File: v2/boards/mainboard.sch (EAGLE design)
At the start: 176 parts, among them IC1 LM2596S-ADJ, IC10 TSOP34830, IC11 DRV8835, IC12 ESP-WROOM-32, IC13 PAM8403, IC2 LM2596S-5.0, IC3 LD1117A, IC4 LM393, IC5 MCP101-300, IC6 TEENSY 3.6, IC7 PCA9634, IC8 PCA9554, IC9 PCA9634, J1 Bat_In, J10 SPI_0, J11 SPI_2, J12 SPI_2, J13 I2C_0, J14 I2C_1, J15 I2C_3, J16 BNO055, J17 Uart_2, J18 Uart_5, J19 Uart_6 (LP), J2 Erw_Pow, J20 BPS, J21 Servo_2, J22 Servo_3, J23 Erw_Servo, J24 Erw_PWM, J25 ESP32_Uart, J26 SPEAKER_L, J27 SPEAKER_R, J28 AUDIO_TEENSY, J29 SWD, J3 I2C0_5V, J30 SWD_KL02, J31 Erw_ENA, J32 Erw_GPIO, J33 Erw_analog, J34 USB_Host, J35 ESP32_PROG, J4 I2C3_5V, J5 Servo_1, J6 H-Bridge Mode, J7 RC5_SEL, J8 SPI_0, J9 SPI_0, SW1 TL32PO, U1 IRL3103, U4 BS108, U5 BS108, U6 BS108, U7 BS108, U8 BS108, U9 BS108, X1 max. 18V

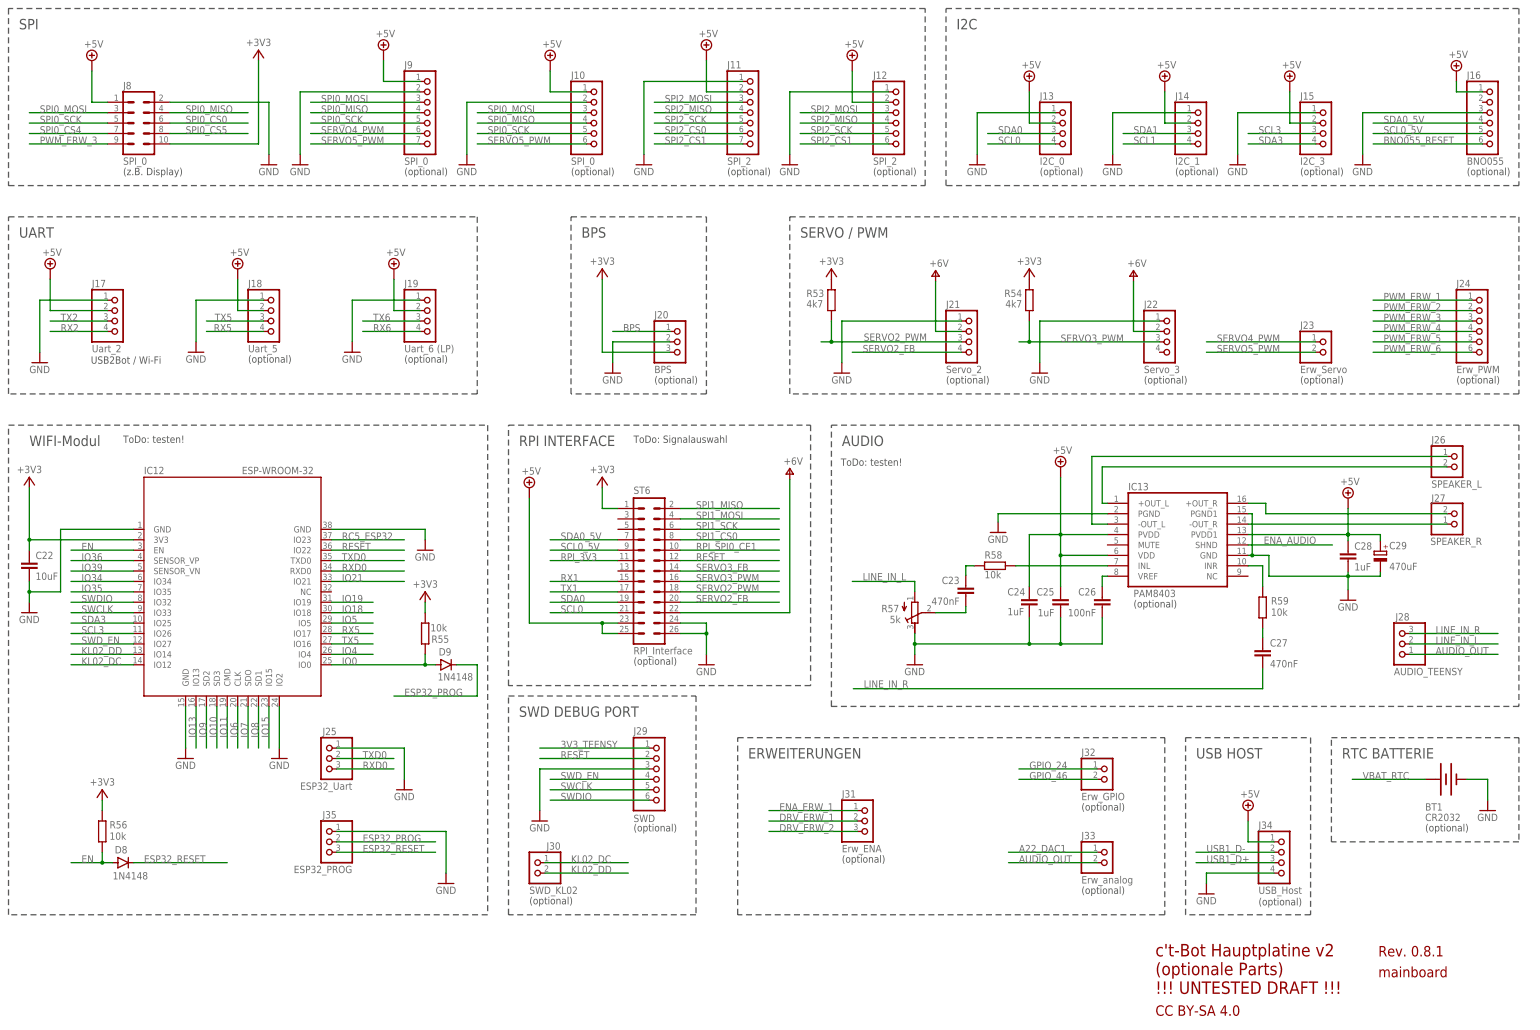
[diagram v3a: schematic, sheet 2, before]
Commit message: ct-bot v2 schematic updated
- optional current measurements added to mainboard
 - schematic drafts for sensor boards
 - pin mapping sheet updated (i2c-bus mapping)
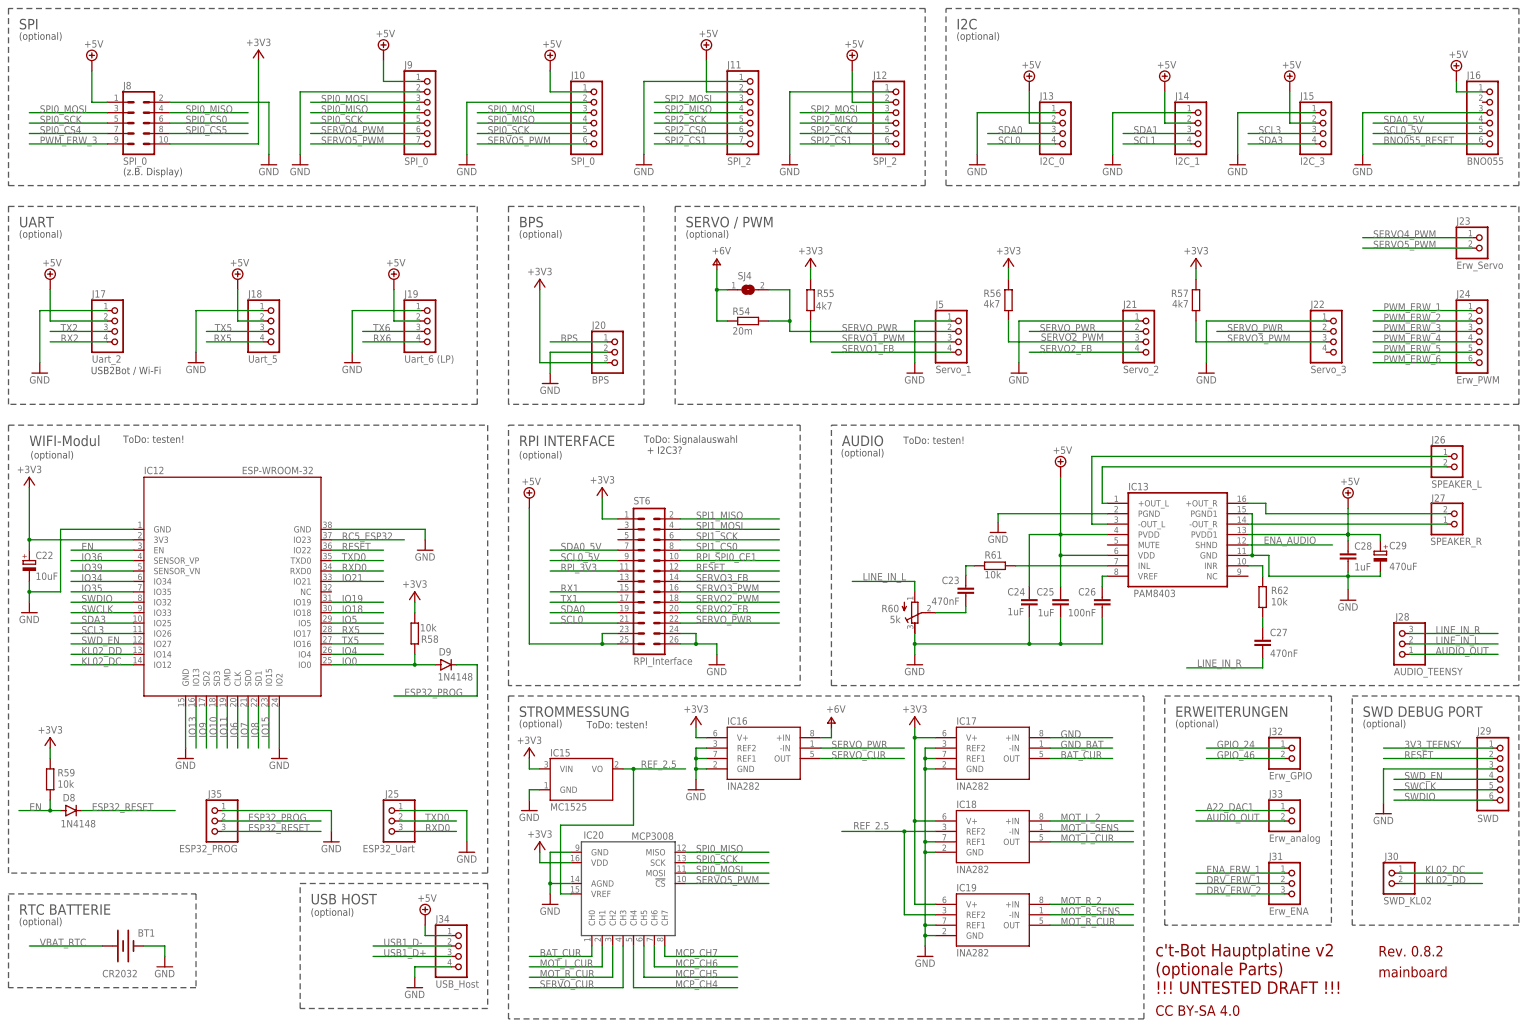
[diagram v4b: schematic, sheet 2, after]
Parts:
- added IC15: MC1525, ct-bot:MC1525TO
- added IC16, IC17, IC18, IC19: INA282, ct-bot:INA28AID
- added IC20: MCP3008, ct-bot:MCP3008SL
- added R51: 4k7, rcl:R-EU_0204/2V
- added R60: 5k, ct-bot:R-TRIMM64W
- added R61: 10k, rcl:R-EU_0204/2V
- added R62: 10k, rcl:R-EU_0204/7
- added SJ1, SJ2, SJ3, SJ4: (no value), jumper:SJ
- C22: device rcl:C-EU025-025X050 -> rcl:CPOL-EUE2.5-5
- J2: value Erw_Pow -> Erw_Pwr
- R10: value 180 -> 120
- R12, R16: value 47k -> 180
- R14, R18: value 180 -> 47k
- R20: value 5k -> 180; device ct-bot:R-TRIMM64W -> rcl:R-EU_0204/2V
- R21: value 10k -> 5k; device rcl:R-EU_0204/2V -> ct-bot:R-TRIMM64W
- R22, R28: value 1M -> 10k
- R23, R29: value 10k -> 1M
- R25, R31: value 15k -> 10k
- R26: value 5k -> 15k; device ct-bot:R-TRIMM64W -> rcl:R-EU_0204/2V
- R27: value 10k -> 5k; device rcl:R-EU_0204/7 -> ct-bot:R-TRIMM64W
- R32: value 100 -> 15k; device rcl:R-EU_0204/2V -> rcl:R-EU_0204/7
- R33: value 470k -> 100
- R35: value 4k7 -> 470k
- R37, R55, R56: value 10k -> 4k7
- R39: value 1k1 -> 10k
- R41: value 1k8 -> 1k1
- R43, R49: value 4k7 -> 1k8
- R44: value 3k9 -> 4k7
- R45: value 220 -> 3k9
- R46: value 590 -> 220
- R47: value 115 -> 590
- R48: value 1k8 -> 115
- R5: value 3k9 0.1% -> 20m; device rcl:R-EU_0204/2V -> rcl:R-EU_R1210
- R52, R53, R54: value 4k7 -> 20m; device rcl:R-EU_0204/2V -> rcl:R-EU_R1210
- R57: value 5k -> 4k7; device ct-bot:R-TRIMM64W -> rcl:R-EU_0204/2V
- R59: device rcl:R-EU_0204/7 -> rcl:R-EU_0204/2V
- R6: value 1k 0.1% -> 3k9 0.1%
- R7: value 390 -> 1k 0.1%
- R8: value 330 -> 390
- R9: value 120 -> 330
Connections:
- new net BAT_CUR: IC17.OUT, IC20.CH0
- new net GND_BAT: IC17.-IN, R5.2, SJ1.2, U1.S
- new net MCP_CH4: IC20.CH4
- new net MCP_CH5: IC20.CH5
- new net MCP_CH6: IC20.CH6
- new net MCP_CH7: IC20.CH7
- new net MOT_L_CUR: IC18.OUT, IC20.CH1
- new net MOT_L_SENS: IC18.-IN, R53.2, SJ3.2, ST5.2
- new net MOT_R_CUR: IC19.OUT, IC20.CH2
- new net MOT_R_SENS: IC19.-IN, R52.2, SJ2.2, ST4.2
- new net REF_2.5: IC15.VO, IC18.REF2, IC19.REF2, IC20.VREF
- new net SERVO_CUR: IC16.OUT, IC20.CH3
- new net SERVO_PWR: IC16.-IN, J21.2, J22.2, J5.2, R54.2, SJ4.2, ST6.22
- net +3V3: now also C22.+, IC15.VIN, IC16.V+, IC17.V+, IC18.V+, IC19.V+, IC20.VDD, R10.2, R13.2, R14.1, R18.2, R21.E, R24.2, R26.2, R27.E, R30.2, R37.2, R41.2, R55.2, R57.2, R58.1, R59.2; no longer C22.1, R12.2, R13.1, R16.2, R20.E, R23.2, R25.2, R26.E, R29.2, R31.2, R39.2, R52.2, R53.2, R54.2, R55.1, R9.2
- net +5V: now also R39.2, R43.2, R51.1, R9.2; no longer R37.2, R41.2, R43.1, R8.2
- net +6V: now also IC16.+IN, R54.1, R6.2, R8.1, SJ4.1; no longer J21.2, J22.2, J5.2, R5.2, R7.1, ST6.22
- net DRV_KANTLED_L: now also R12.2; no longer R11.2
- net DRV_KANTLED_R: now also R16.1; no longer R15.1
- net DRV_LINE_L: now also R20.2; no longer R19.2
- net DRV_LINE_R: now also R19.2; no longer R18.2
- net DRV_RADLED_L: now also R11.2; no longer R10.2
- net DRV_RADLED_R: now also R15.1; no longer R14.1
- net EN: now also R59.1; no longer R56.1
- net ENC_L: now also R25.2, R26.1; no longer R24.2, R25.1
- net ENC_R: now also R31.2, R32.1; no longer R30.2, R31.1
- net GND: now also C22.-, IC15.GND, IC16.GND, IC16.REF1, IC16.REF2, IC17.+IN, IC17.GND, IC17.REF1, IC17.REF2, IC18.GND, IC18.REF1, IC19.GND, IC19.REF1, IC20.AGND, IC20.GND, R21.A, R27.A, R5.1, R60.E, R7.1, SJ1.1; no longer C22.2, R20.A, R26.A, R57.E, R6.1, U1.S
- net IO0: now also R58.2; no longer R55.2
- net KANTE_L: now also R13.1; no longer R12.1
- net KANTE_R: now also R14.2; no longer R13.2
- net LDR_L: now also R34.1; no longer R33.1
- net LDR_R: now also R35.1; no longer R34.1
- net LINE_IN_L: now also R60.A; no longer R57.A
- net LINIE_L: now also R18.1; no longer R17.1
- net LINIE_R: now also R17.1; no longer R16.1
- net MOT_L_2: now also IC18.+IN, R53.1, SJ3.1; no longer ST5.2
- net MOT_R_2: now also IC19.+IN, R52.1, SJ2.1; no longer ST4.2
- net N$1: now also R19.1; no longer R18.1
- net N$10: now also R31.1; no longer R30.1
- net N$11: now also R9.1; no longer R8.1
- net N$2: now also R10.1; no longer R9.1
- net N$20: now also R44.2; no longer R43.2
- net N$21: now also R45.2; no longer R44.2
- net N$22: now also R46.2; no longer R45.2
- net N$23: now also R47.2; no longer R46.2
- net N$24: now also R48.2; no longer R47.2
- net N$25: now also R49.2; no longer R48.2
- net N$26: now also R50.2; no longer R49.2
- net N$27: now also R51.2; no longer R50.2
- net N$28: now also R33.1; no longer R32.1
- net N$30: now also R20.1; no longer R19.1
- net N$34: now also R21.S, R22.1; no longer R20.S, R21.1
- net N$35: now also R22.2, R23.1; no longer R21.2, R22.1
- net N$36: now also R27.S, R28.1; no longer R26.S, R27.1
- net N$37: now also R28.2, R29.1; no longer R27.2, R28.1
- net N$40: now also R61.1; no longer R58.1
- net N$41: now also R61.2; no longer R58.2
- net N$42: now also R60.S; no longer R57.S
- net N$45: now also R15.2; no longer R14.2
- net N$46: now also R62.1; no longer R59.1
- net N$47: now also R11.1; no longer R10.1
- net N$48: now also R62.2; no longer R59.2
- net N$5: now also R25.1; no longer R24.1
- net N$51: now also R12.1; no longer R11.1
- net N$53: now also R16.2; no longer R15.2
- net N$8: now also R8.2; no longer R7.2
- net N$9: now also R6.1, R7.2; no longer R5.1, R6.2
- net RAD_L: now also R23.2, R24.1; no longer R22.2, R23.1
- net RAD_R: now also R29.2, R30.1; no longer R28.2, R29.1
- net SCL0: now also R37.1; no longer R36.1
- net SCL0_5V: now also R39.1; no longer R38.1
- net SCL3: now also R41.1; no longer R40.1
- net SCL3_5V: now also R43.1; no longer R42.1
- net SDA0: now also R36.1; no longer R35.1
- net SDA0_5V: now also R38.1; no longer R37.1
- net SDA3: now also R40.1; no longer R39.1
- net SDA3_5V: now also R42.1; no longer R41.1
- net SERVO1_PWM: now also R55.1; no longer R52.1
- net SERVO2_PWM: now also R56.1; no longer R53.1
- net SERVO3_PWM: now also R57.1; no longer R54.1
- net SERVO5_PWM: now also IC20.!CS
- net SPI0_MISO: now also IC20.MISO
- net SPI0_MOSI: now also IC20.MOSI
- net SPI0_SCK: now also IC20.SCK
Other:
- note added: "Motoren"
- note added: "Rev. 0.8.2"
- note added: "STROMMESSUNG"
- note added: "ToDo: Signalauswahl + I2C3?"
- note removed: "Aktuatoren"
- note removed: "Rev. 0.8.1"
- note removed: "ToDo: Signalauswahl"
- moved on the sheet: BT1, C1, C27, D1, D2, D8, J1, J17, J18, J19, J2, J20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

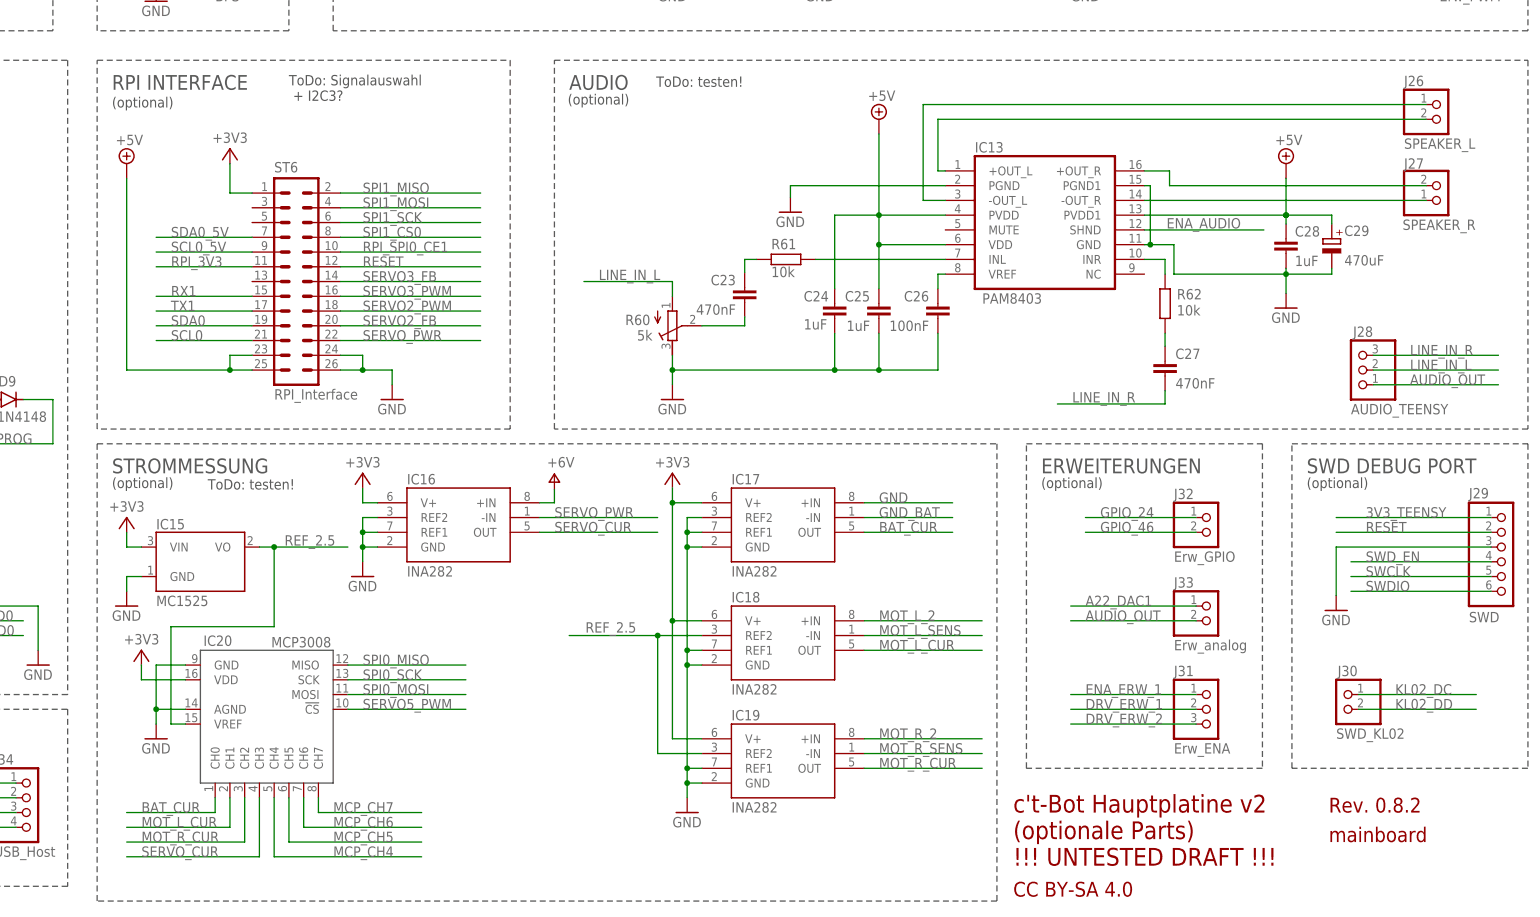
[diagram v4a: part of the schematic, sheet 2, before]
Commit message: ct-bot v2 schematic updated according to todo list
- analog ground
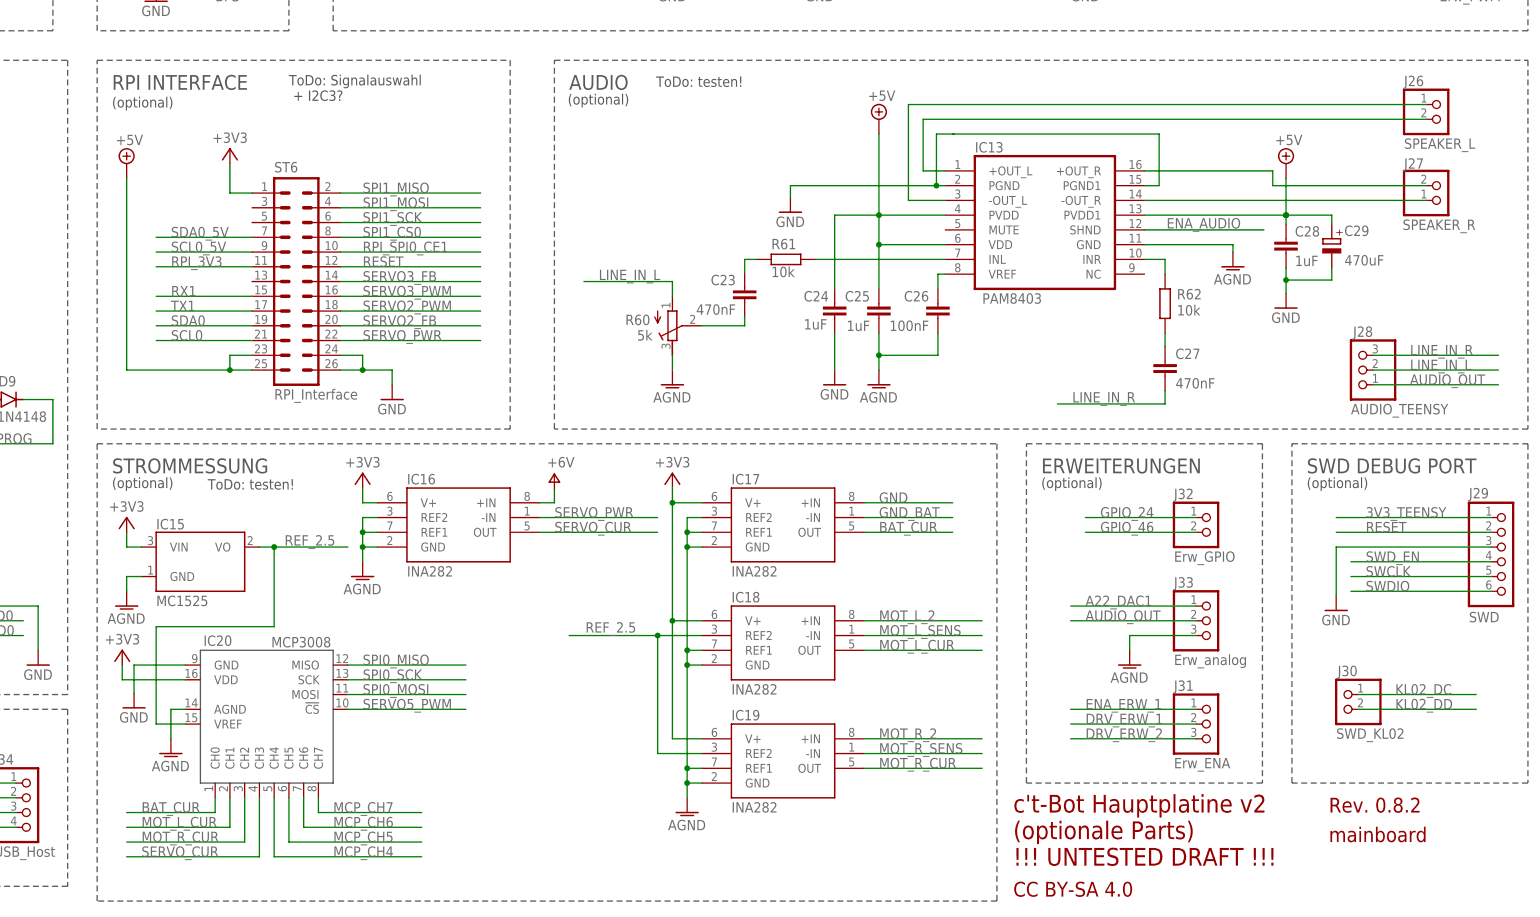
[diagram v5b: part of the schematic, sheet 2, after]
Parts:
- IC10: value TSOP34830 -> DRV8835; device ct-bot:TSOP34830 -> ct-bot:DRV8835THROUGHHOLE
- IC11: value DRV8835 -> TSOP324; device ct-bot:DRV8835THROUGHHOLE -> ct-bot:TSOP324
- J33: device ct-bot:PINHD-1X2 -> ct-bot:PINHD-1X3
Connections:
- new net AGND: C25.2, C26.2, IC13.GND, IC15.GND, IC16.GND, IC16.REF1, IC16.REF2, IC17.GND, IC17.REF1, IC17.REF2, IC18.GND, IC18.REF1, IC19.GND, IC19.REF1, IC20.AGND, IC6.AGND, J33.3, R60.E
- net +3V3: now also IC11.VS; no longer IC10.VS
- net +5V: now also IC10.VCC; no longer IC11.VCC
- net +6V: now also IC10.VIN; no longer IC11.VIN
- net FERNBED: now also IC11.OUT; no longer IC10.OUT
- net GND: now also IC10.LGND, IC10.MGND, IC11.GND; no longer C25.2, C26.2, IC10.GND, IC11.LGND, IC11.MGND, IC13.GND, IC15.GND, IC16.GND, IC16.REF1, IC16.REF2, IC17.GND, IC17.REF1, IC17.REF2, IC18.GND, IC18.REF1, IC19.GND, IC19.REF1, IC20.AGND, IC6.AGND, R60.E
- net MOT_L_1: now also IC10.AOUT1; no longer IC11.AOUT1
- net MOT_L_2: now also IC10.AOUT2; no longer IC11.AOUT2
- net MOT_L_DIR: now also IC10.APHASE; no longer IC11.APHASE
- net MOT_L_PWM: now also IC10.AENBL; no longer IC11.AENBL
- net MOT_R_1: now also IC10.BOUT1; no longer IC11.BOUT1
- net MOT_R_2: now also IC10.BOUT2; no longer IC11.BOUT2
- net MOT_R_DIR: now also IC10.BPHASE; no longer IC11.BPHASE
- net MOT_R_PWM: now also IC10.BENBL; no longer IC11.BENBL
- net N$3: now also IC10.MODE; no longer IC11.MODE
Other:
- moved on the sheet: C18, J31
